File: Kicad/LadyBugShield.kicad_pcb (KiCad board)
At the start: 2 copper layers, 81.3 x 55.3 mm, 55 parts, among them P1 CONN_6, P2 CONN_2, P3 BNC, P4 BNC, Q1 TIP122, Q2 TIP122, Q3 TIP122, U1 MCP6244, U2 MCP6242, U3 MC78L05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

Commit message: updated to Diode SOD-123 footprint
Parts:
- D1, D4, D5, D6, D7, D8: footprint SM1206 -> SOD-123
- moved D1 6.62 mm to (166.9, 94.4), turned to 180 degrees
- moved D6 4.53 mm to (219.8, 85.8), turned to 270 degrees
- moved D5 1.88 mm to (165.9, 90.4), turned to 180 degrees
- moved D7 0.67 mm to (217.4, 85.8), turned to 90 degrees
- moved D4 0.14 mm to (198.8, 86.7)
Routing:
- net VClean: track 290.1 -> 282.0 mm
- net /Pumps/SW_Pump1: track 31.9 -> 25.9 mm
- net /EC/DD: track 35.3 -> 29.9 mm, vias 3 -> 2
- net /EC/RVin-: track 12.9 -> 17.3 mm
- net /Pumps/SW_Pump2: track 26.0 -> 27.2 mm

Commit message: updates based on reviewing layout
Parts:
- removed the ? at (186.8, 78.1)
- removed TP3, TP4: CONN_1, LB_CONN_1
- removed ~: ~, OSHW_CU
- removed ~: ~, OSHW_SM
- added ?: , LadybugLogo, F.Cu at (186.0, 88.0)
- added ?: , OSHW_SM, B.SilkS at (185.4, 98.7)
- D2: footprint SM1206 -> SOD-123
- moved TP1 11.2 mm to (224.2, 67.7)
- moved D2 1.30 mm to (161.5, 84.2), turned to 180 degrees
- moved D5 1.16 mm to (165.1, 89.6), turned to 270 degrees
- moved TP2 0.93 mm to (231.4, 92.4)
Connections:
- P1 pad 5: /Pumps/SW_Pump3 -> VClean
- P1 pad 6: VClean -> /Pumps/SW_Pump3
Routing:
- net /Pumps/SW_Pump3: track 23.6 -> 17.4 mm
- net VGND: track 146.5 -> 141.1 mm
- net /pH/pH_ProbeIN: track 40.4 -> 38.1 mm
- net /Pumps/SW_Pump2: track 27.2 -> 26.0 mm
- net /EC/EC_ProbeIN: track 28.6 -> 29.4 mm
- net VClean: track 282.0 -> 282.3 mm, vias 1 -> 2

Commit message: AlphaV1 build that was sent to OshPark
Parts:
- moved C5 9.32 mm to (204.5, 88.6), turned to 180 degrees
- moved R14 6.94 mm to (203.9, 92.2), turned to 270 degrees
- moved R3 4.90 mm to (216.4, 92.7), turned to 180 degrees
- moved P1 4.66 mm to (161.2, 103.9)
- moved D1 4.25 mm to (171.1, 93.7)
- moved C6 4.24 mm to (204.0, 79.1)
- moved D5 3.68 mm to (168.4, 91.2), turned to 0 degrees
- moved P4 3.02 mm to (225.7, 104.2)
- moved P3 2.68 mm to (225.5, 79.0)
- moved TP2 2.54 mm to (228.9, 93.0)
- moved P2 2.54 mm to (234.5, 88.4)
- moved C12 2.47 mm to (174.5, 110.1)
- moved R5 2.47 mm to (168.5, 110.1)
- moved C13 2.47 mm to (171.5, 110.2)
- moved D3 2.47 mm to (164.3, 108.8)
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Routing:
- net /EC/f1: track 34.4 -> 2.79 mm
- net VClean: track 282.3 -> 293.2 mm, vias 2 -> 0
- net VGND: track 141.1 -> 149.5 mm
- net /pH/pH_ProbeIN: track 38.1 -> 33.8 mm
- net /EC/EC_ProbeIN: track 29.4 -> 25.8 mm
- net AC_Shrunk: track 17.7 -> 14.4 mm, vias 2 -> 3
- net /EC/W_Vout: track 15.2 -> 18.5 mm
- net /Pumps/SW_Pump3: track 17.4 -> 14.5 mm
- net /Pumps/SW_Pump1: track 25.9 -> 28.2 mm
- net /EC/W_Vin+: track 11.4 -> 9.24 mm
- net /Pumps/SW_Pump2: track 26.0 -> 27.5 mm
- net /EC/G1: track 13.5 -> 12.3 mm
- net /EC/W_Vin-: track 17.6 -> 18.2 mm
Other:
- board text added: "Alpha V1"
- board text added: "bitknitting.wordpress.com"

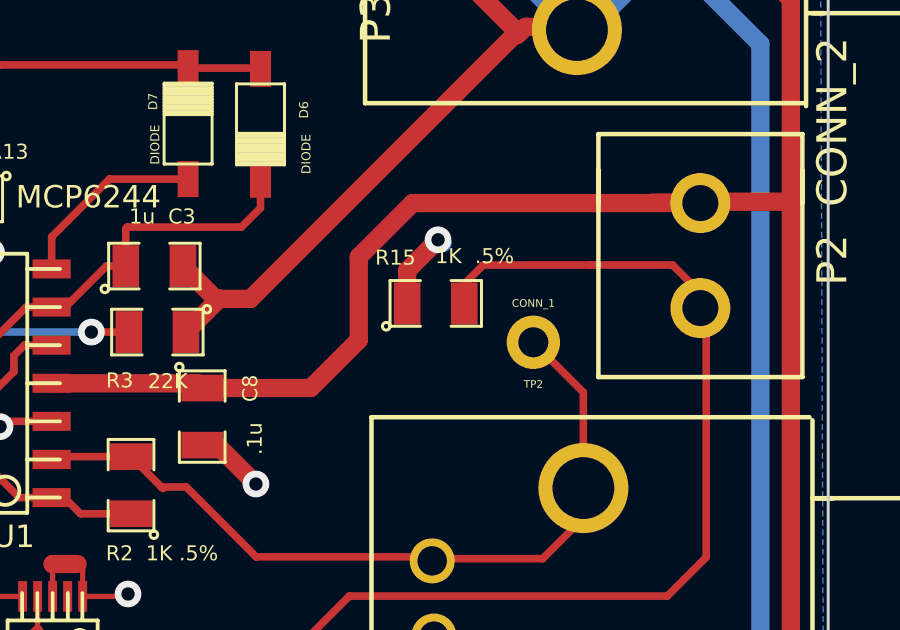
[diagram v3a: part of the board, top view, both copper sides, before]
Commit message: Added Thermistor Arduino Sketch.  Changed schematic/layout: label of R15 from 1K to 10K
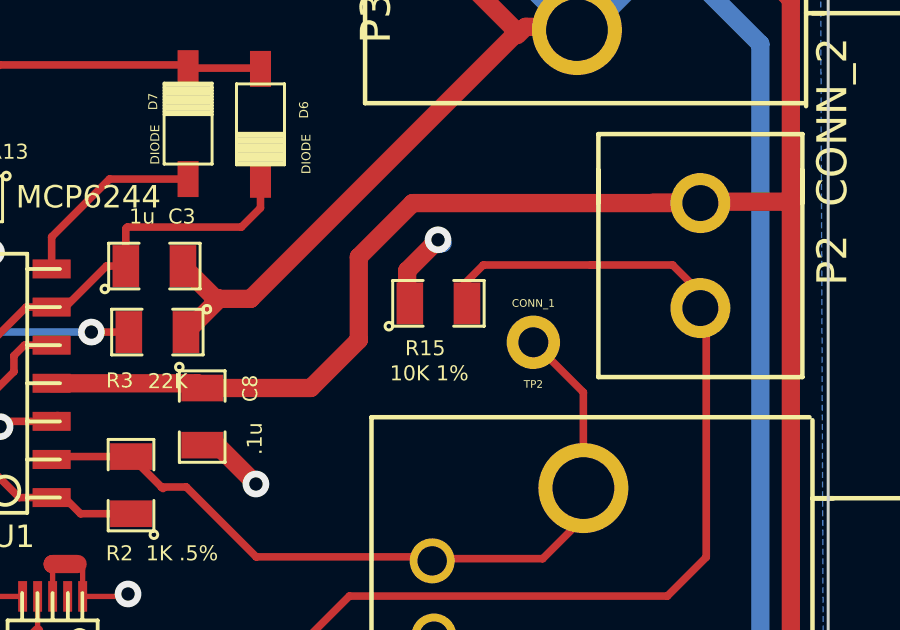
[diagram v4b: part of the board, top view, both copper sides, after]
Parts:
- R15: value 1K .5% -> 10K 1%
- moved R15 0.09 mm to (225.8, 91.7)
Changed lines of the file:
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@@
     (links 111)
     (no_connects 0)
-    (area 150.920999 63.130999 259.401141 118.820401)
+    (area 157.422379 63.449999 238.810001 118.820401)
     (thickness 1.6)
     (drawings 18)
@@
       (layers F.Cu F.Paste F.Mask)
       (net 26 N-0000050)
-    )
-    (model smd/chip_cms.wrl
-      (at (xyz 0 0 0))
-      (scale (xyz 0.1 0.1 0.1))
-      (rotate (xyz 0 0 0))
-    )
-  )
-  (module SM0805 (layer F.Cu)
-    (at 225.679 91.7448)
-    (attr smd)
-    (fp_text reference R15 (at -1.3462 -1.524) (layer F.SilkS)
-      (effects (font (size 0.50038 0.50038) (thickness 0.10922)))
-    )
-    (fp_text value "1K  .5%" (at 1.2954 -1.5748) (layer F.SilkS)
-      (effects (font (size 0.50038 0.50038) (thickness 0.10922)))
-    )
-    (fp_circle (center -1.651 0.762) (end -1.651 0.635) (layer F.SilkS) (width 0.09906))
-    (fp_line (start -0.508 0.762) (end -1.524 0.762) (layer F.SilkS) (width 0.09906))
-    (fp_line (start -1.524 0.762) (end -1.524 -0.762) (layer F.SilkS) (width 0.09906))
-    (fp_line (start -1.524 -0.762) (end -0.508 -0.762) (layer F.SilkS) (width 0.09906))
-    (fp_line (start 0.508 -0.762) (end 1.524 -0.762) (layer F.SilkS) (width 0.09906))
-    (fp_line (start 1.524 -0.762) (end 1.524 0.762) (layer F.SilkS) (width 0.09906))
-    (fp_line (start 1.524 0.762) (end 0.508 0.762) (layer F.SilkS) (width 0.09906))
-    (pad 1 smd rect (at -0.9525 0) (size 0.889 1.397)
-      (layers F.Cu F.Paste F.Mask)
-      (net 25 GND)
-    )
-    (pad 2 smd rect (at 0.9525 0) (size 0.889 1.397)
-      (layers F.Cu F.Paste F.Mask)
-      (net 7 /DigitalAccess/Therm_AIN)
     )
     (model smd/chip_cms.wrl
@@
     )
   )
+  (module SM0805 (layer F.Cu)
+    (at 225.7679 91.74226)
+    (attr smd)
+    (fp_text reference R15 (at -0.43942 1.4986) (layer F.SilkS)
+      (effects (font (size 0.50038 0.50038) (thickness 0.10922)))
+    )
+    (fp_text value "10K 1%" (at -0.30734 2.33426) (layer F.SilkS)
+      (effects (font (size 0.50038 0.50038) (thickness 0.10922)))
+    )
+    (fp_circle (center -1.651 0.762) (end -1.651 0.635) (layer F.SilkS) (width 0.09906))
+    (fp_line (start -0.508 0.762) (end -1.524 0.762) (layer F.SilkS) (width 0.09906))
+    (fp_line (start -1.524 0.762) (end -1.524 -0.762) (layer F.SilkS) (width 0.09906))
+    (fp_line (start -1.524 -0.762) (end -0.508 -0.762) (layer F.SilkS) (width 0.09906))
+    (fp_line (start 0.508 -0.762) (end 1.524 -0.762) (layer F.SilkS) (width 0.09906))
+    (fp_line (start 1.524 -0.762) (end 1.524 0.762) (layer F.SilkS) (width 0.09906))
+    (fp_line (start 1.524 0.762) (end 0.508 0.762) (layer F.SilkS) (width 0.09906))
+    (pad 1 smd rect (at -0.9525 0) (size 0.889 1.397)
+      (layers F.Cu F.Paste F.Mask)
+      (net 25 GND)
+    )
+    (pad 2 smd rect (at 0.9525 0) (size 0.889 1.397)
+      (layers F.Cu F.Paste F.Mask)
+      (net 7 /DigitalAccess/Therm_AIN)
+    )
+    (model smd/chip_cms.wrl
+      (at (xyz 0 0 0))
+      (scale (xyz 0.1 0.1 0.1))
+      (rotate (xyz 0 0 0))
+    )
+  )
   (gr_text bitknitting.wordpress.com (at 198.2 82.8) (layer B.SilkS)
     (effects (font (size 1.5 1.5) (thickness 0.3)) (justify mirror))
@@
   (segment (start 211.1248 83.7946) (end 209.677 85.2424) (width 0.254) (layer F.Cu) (net 9))
   (segment (start 217.5764 83.7946) (end 211.1248 83.7946) (width 0.254) (layer F.Cu) (net 9))
-  (segment (start 230.6 97.9) (end 230.6 94.70746) (width 0.254) (layer F.Cu) (net 10) (status 400000))
-  (segment (start 230.6 94.70746) (end 228.93274 93.0402) (width 0.254) (layer F.Cu) (net 10) (status 800000))
+  (segment (start 230.6 97.9) (end 230.6 94.70746) (width 0.254) (layer F.Cu) (net 10))
+  (segment (start 230.6 94.70746) (end 228.93274 93.0402) (width 0.254) (layer F.Cu) (net 10))
   (segment (start 216.53567 97.86433) (end 217.36433 97.86433) (width 0.254) (layer F.Cu) (net 10))
   (segment (start 219.69284 100.19284) (end 225.38182 100.19284) (width 0.254) (layer F.Cu) (net 10))
@@
   (segment (start 213.83752 98.7552) (end 215.52154 98.7552) (width 0.254) (layer F.Cu) (net 24))
   (segment (start 213.29904 98.21672) (end 213.83752 98.7552) (width 0.254) (layer F.Cu) (net 24))
+  (segment (start 224.7265 91.7448) (end 224.7265 90.6526) (width 0.6096) (layer F.Cu) (net 25))
+  (segment (start 225.8695 89.7382) (end 225.9076 89.7382) (width 0.6096) (layer B.Cu) (net 25))
+  (segment (start 225.7552 89.6239) (end 225.8695 89.7382) (width 0.6096) (layer B.Cu) (net 25))
+  (via (at 225.7552 89.6239) (size 0.889) (layers F.Cu B.Cu) (net 25))
+  (segment (start 224.7265 90.6526) (end 225.7552 89.6239) (width 0.6096) (layer F.Cu) (net 25))
   (segment (start 213.90864 101.5111) (end 215.3412 101.5111) (width 0.1778) (layer F.Cu) (net 25))
   (via (at 215.42248 101.42982) (size 0.889) (layers F.Cu B.Cu) (net 25))
@@
   (via (at 199.5297 75.3618) (size 0.889) (layers F.Cu B.Cu) (net 25))
   (segment (start 199.78878 75.10272) (end 199.5297 75.3618) (width 0.6096) (layer F.Cu) (net 25))
-  (segment (start 224.7265 91.7448) (end 224.7265 90.6526) (width 0.6096) (layer F.Cu) (net 25))
-  (segment (start 225.8695 89.7382) (end 225.9076 89.7382) (width 0.6096) (layer B.Cu) (net 25))
-  (segment (start 225.7552 89.6239) (end 225.8695 89.7382) (width 0.6096) (layer B.Cu) (net 25))
-  (via (at 225.7552 89.6239) (size 0.889) (layers F.Cu B.Cu) (net 25))
-  (segment (start 224.7265 90.6526) (end 225.7552 89.6239) (width 0.6096) (layer F.Cu) (net 25))
   (segment (start 217.8939 96.4692) (end 218.3892 96.4692) (width 0.6096) (layer F.Cu) (net 25))
   (via (at 219.6846 97.7646) (size 0.889) (layers F.Cu B.Cu) (net 25))

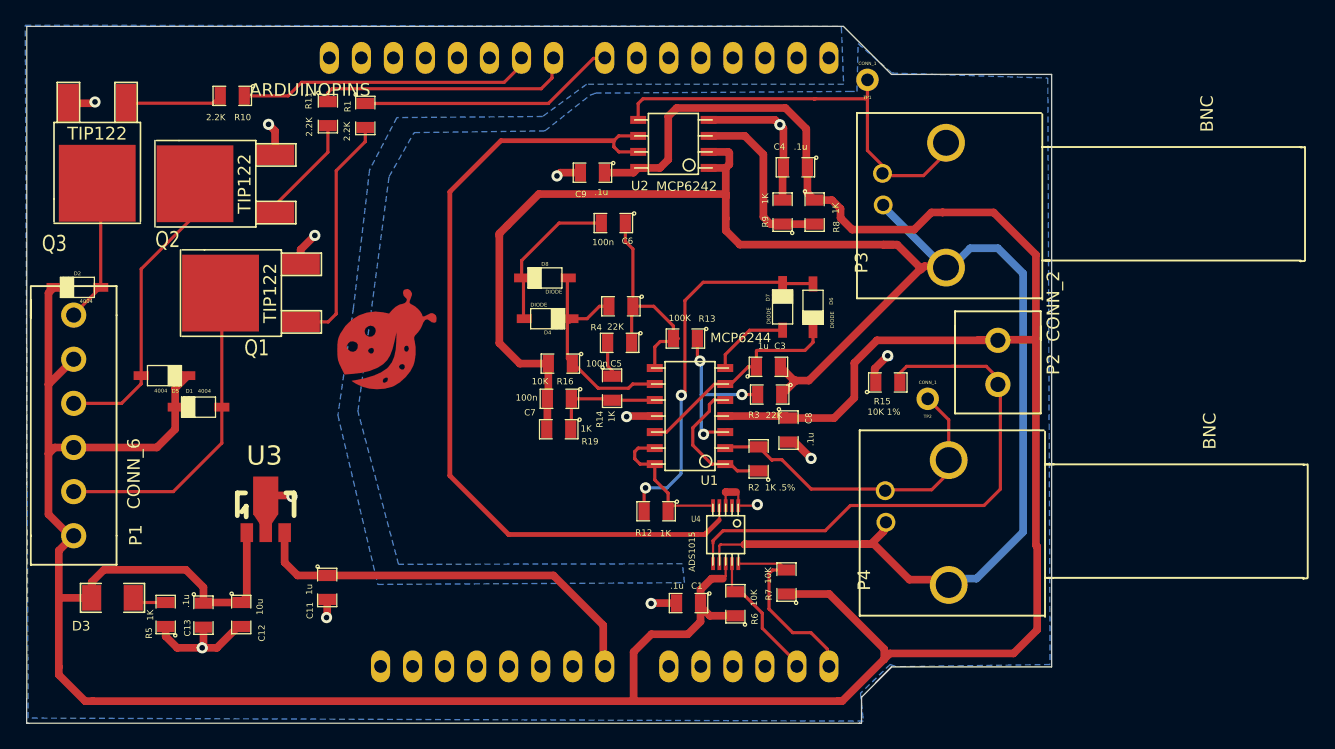
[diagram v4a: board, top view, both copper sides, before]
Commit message: fixed BNC connector circuit...still needs final review
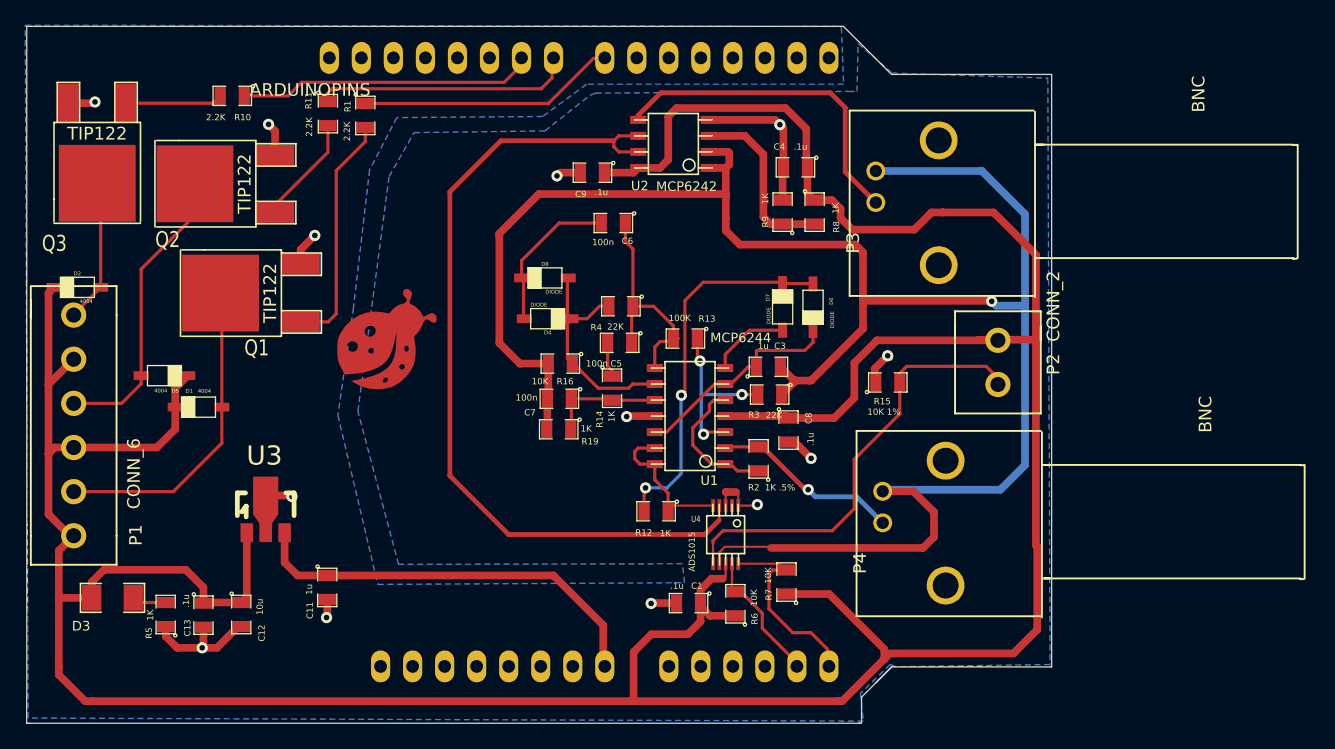
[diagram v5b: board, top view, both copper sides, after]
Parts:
- removed TP1, TP2: CONN_1, LB_CONN_1
- moved P3 1.70 mm to (224.8, 77.5)
- moved P4 1.37 mm to (225.4, 102.9)
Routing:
- net /EC/EC_ProbeIN: track 25.8 -> 15.0 mm, vias 0 -> 1
- net VGND: track 149.5 -> 158.7 mm, vias 0 -> 1
- net /DigitalAccess/Therm_AIN: track 44.7 -> 35.9 mm
- net /pH/pH_ProbeIN: track 33.8 -> 26.5 mm

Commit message: layout for Alpha 2
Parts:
- removed D8: DIODE, SOD-123
- removed R19: 1K, SM0805
- added C2: .1u, SM0805, F.Cu at (218.6, 92.7)
- added Q4: MOSFET_N, LB_MOSFET, F.Cu at (195.9, 100.0)
- added R17: 1K .5%, SM0805, F.Cu at (218.7, 99.0)
- added U5: MCP6244, LB_MCP6244, F.Cu at (203.5, 94.8)
- C3: value 1u -> .1u
- C5, C6, C7: value 100n -> .1u
- R12: value 1K -> 22K
- R13: value 100K -> 1K
- R14: value 1K -> 10K
- R2: value 1K .5% -> 10K
- R3: value 22K -> 1K
- R4: value 22K -> 10K
- U1: value MCP6244 -> 74LVC1G53; footprint LB_MCP6244 -> so-8
- moved D7 21.7 mm to (196.3, 91.0), turned to 270 degrees
- moved C6 16.3 mm to (208.6, 94.7), turned to 90 degrees
- moved R12 14.2 mm to (208.4, 87.8)
- moved D4 13.4 mm to (210.1, 79.5), turned to 180 degrees
- moved C4 12.7 mm to (206.1, 71.8)
- moved R8 12.6 mm to (208.0, 74.2), turned to 0 degrees
- moved R2 10.9 mm to (213.1, 108.5)
- moved C5 10.7 mm to (214.0, 93.5), turned to 270 degrees
- moved D6 10.5 mm to (210.1, 81.8), turned to 0 degrees
- moved R9 9.48 mm to (208.1, 76.5), turned to 180 degrees
- moved C1 6.67 mm to (216.6, 109.0)
- moved R6 6.55 mm to (220.0, 111.0), turned to 180 degrees
- moved R16 6.32 mm to (203.4, 85.0)
- moved U2 6.19 mm to (214.9, 73.6), turned to 0 degrees
- moved U1 6.01 mm to (211.0, 100.3), turned to 0 degrees
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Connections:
- ARD1 pad 6: (no net) -> /Arduino/FET_pin
- ARD1 pad 7: (no net) -> /Arduino/MUX_enable_pin
- ARD1 pad 8: (no net) -> /Arduino/MUX_out_pin
- C3 pad 1: /EC/RVin- -> /EC/AC/W_Vout
- C3 pad 2: VGND -> /EC/AC/G1
- C5 pad 1: /EC/W_Vout -> /EC/AC/W_Vout
- C5 pad 2: /EC/f1 -> /EC/AC/f1
- C6 pad 1: /EC/W_Vout -> VClean
- C6 pad 2: /EC/G1 -> GND
- C7 pad 1: /EC/W_Vin+ -> /EC/Rectify/RVin-
- D4 pad 1: /EC/G1 -> /EC/AC/G1
- D4 pad 2: /EC/W_Vin- -> /EC/AC/W_Vin-
- D6 pad 1: /EC/DD -> /EC/AC/W_Vin-
- D6 pad 2: /EC/RVin- -> /EC/AC/G1
- D7 pad 1: /EC/R_Vout -> /EC/Rectify/R_Vout
- D7 pad 2: /EC/DD -> /EC/Rectify/RVin-
- R12 pad 1: /DigitalAccess/EC_AIN -> /EC/AC/W_Vout
- R12 pad 2: /EC/DD -> /EC/AC/W_Vin-
- R13 pad 1: AC_Shrunk -> /EC/AC/f1
- R13 pad 2: /EC/W_Vout -> /EC/AC/W_Vin+
- R14 pad 1: /EC/f1 -> /EC/AC/EC_Vin+
- R14 pad 2: /EC/W_Vin+ -> /EC/AC/W_Vout
- R16 pad 1: /EC/W_Vin- -> VGND
- R16 pad 2: VGND -> /EC/AC/EC_Vin+
- R2 pad 1: EC_Signal -> /Arduino/MUX_enable_pin
- R2 pad 2: /EC/EC_ProbeIN -> GND
- R3 pad 1: VGND -> /EC/AC/W_Vin+
- R3 pad 2: AC_Shrunk -> VGND
- R4 pad 1: /EC/W_Vout -> /EC/AC/W_Vin-
- R4 pad 2: /EC/W_Vin- -> VGND
- U1 pad 1: EC_Signal -> /EC/Rectify/Signal
- U1 pad 2: /EC/EC_ProbeIN -> /Arduino/MUX_enable_pin
- U1 pad 3: AC_Shrunk -> GND
- U1 pad 4: VClean -> GND
- U1 pad 5: EC_Signal -> /Arduino/MUX_out_pin
- U1 pad 6: /EC/RVin- -> /EC/ECGain/EC_DCv
- U1 pad 7: /EC/R_Vout -> /EC/AC/EC_Vin+
- U1 pad 8: /EC/W_Vout -> VClean
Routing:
- net /EC/DD: track 29.9 -> 0.00 mm, vias 2 -> 0
- net /Arduino/FET_pin: track 0.00 -> 21.3 mm
- net /EC/AC/W_Vin-: track 0.00 -> 20.7 mm
- net /EC/Rectify/Signal: track 0.00 -> 20.6 mm
- net /EC/AC/EC_Vin+: track 0.00 -> 20.6 mm
- net /EC/Rectify/RVin-: track 0.00 -> 19.3 mm
- net /Arduino/MUX_out_pin: track 0.00 -> 18.8 mm, vias 0 -> 2
- net /EC/W_Vout: track 18.5 -> 0.00 mm
- net /EC/W_Vin-: track 18.2 -> 0.00 mm
- net /EC/RVin-: track 17.2 -> 0.00 mm
- net /EC/AC/W_Vin+: track 0.00 -> 16.8 mm
- net /pH/pH_ProbeIN: track 26.5 -> 10.9 mm
- net /DigitalAccess/pH_AIN: track 66.8 -> 81.9 mm, vias 0 -> 2
- net /EC/AC/W_Vout: track 0.00 -> 15.0 mm
- net AC_Shrunk: track 14.4 -> 0.00 mm, vias 3 -> 0
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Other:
- board text added: "Alpha V2"
- board text removed: "Alpha V1"
